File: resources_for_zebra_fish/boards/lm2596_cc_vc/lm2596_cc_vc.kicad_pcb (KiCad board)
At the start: 2 copper layers, 72.4 x 78.7 mm, 30 parts, among them J1 Vin, J2 Conn_Coaxial, J3 external_on/off, J4 to_mosfet, J5 red_vout, U1 LM2596T-3.3, U2 LM2596T-ADJ, U3 MCP602

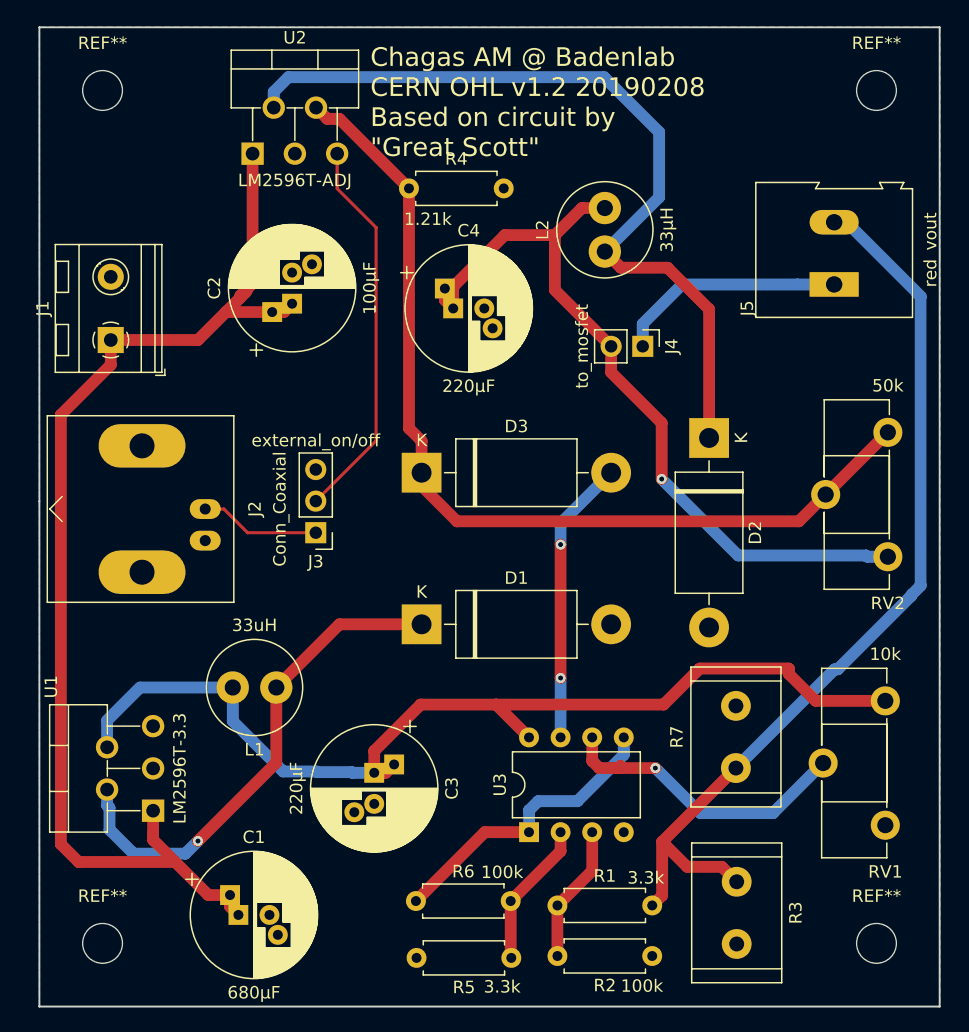
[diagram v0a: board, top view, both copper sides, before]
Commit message: new board: power supply and sync to led in one
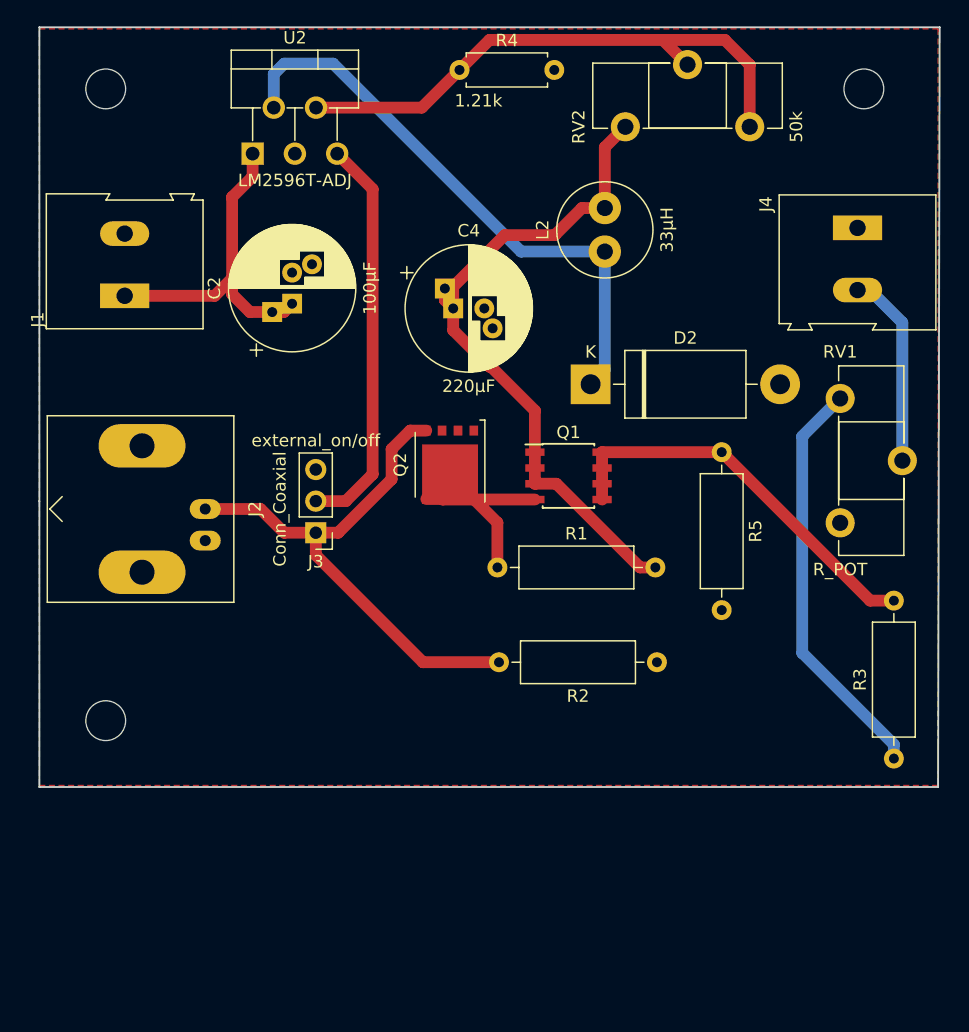
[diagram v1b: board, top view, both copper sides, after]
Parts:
- removed C1: 680µF, Capacitor_THT:CP_Radial_D10.0mm_P2.50mm_P5.00mm
- removed C3: 220µF, Capacitor_THT:CP_Radial_D10.0mm_P2.50mm_P5.00mm
- removed D1, D3: 1N5822, Diode_THT:D_DO-201AD_P15.24mm_Horizontal
- removed J5: red_vout, TerminalBlock:TerminalBlock_Altech_AK300-2_P5.00mm
- removed L1: 33uH, Inductor_THT:L_Radial_D7.5mm_P3.50mm_Fastron_07P
- removed R6: 100k, Resistor_THT:R_Axial_DIN0207_L6.3mm_D2.5mm_P7.62mm_Horizontal
- removed R7: 0.1, Resistor_THT:R_Radial_Power_L11.0mm_W7.0mm_P5.00mm
- removed the REF** at (49.5, 141.0)
- removed the REF** at (111.8, 141.0)
- removed the REF** at (111.8, 72.4)
- removed the REF** at (49.5, 72.4)
- removed U1: LM2596T-3.3, Package_TO_SOT_THT:TO-220-5_P3.4x3.7mm_StaggerOdd_Lead3.8mm_Vertical
- removed U3: MCP602, Package_DIP:DIP-8_W7.62mm
- added Q1: pchannel, Package_SO:SOIC-8_3.9x4.9mm_P1.27mm, F.Cu at (87.0, 103.4)
- added Q2: nchannel, Package_TO_SOT_SMD:TDSON-8-1, F.Cu at (77.5, 102.5)
- added REF**: MountingHole_3.2mm_M3_DIN965, MountingHole:MountingHole_3.2mm_M3_DIN965, F.Cu at (49.8, 123.1)
- added REF**: MountingHole_3.2mm_M3_DIN965, MountingHole:MountingHole_3.2mm_M3_DIN965, F.Cu at (110.7, 72.3)
- added REF**: MountingHole_3.2mm_M3_DIN965, MountingHole:MountingHole_3.2mm_M3_DIN965, F.Cu at (49.8, 72.3)
- J1: footprint TerminalBlock_RND:TerminalBlock_RND_205-00232_1x02_P5.08mm_Horizontal -> TerminalBlock:TerminalBlock_Altech_AK300-2_P5.00mm
- J4: value to_mosfet -> Vout; footprint Connector_PinHeader_2.54mm:PinHeader_1x02_P2.54mm_Vertical -> TerminalBlock:TerminalBlock_Altech_AK300-2_P5.00mm
- R1: value 3.3k -> 10k; footprint Resistor_THT:R_Axial_DIN0207_L6.3mm_D2.5mm_P7.62mm_Horizontal -> Resistor_THT:R_Axial_DIN0309_L9.0mm_D3.2mm_P12.70mm_Horizontal
- R2: value 100k -> 10k; footprint Resistor_THT:R_Axial_DIN0207_L6.3mm_D2.5mm_P7.62mm_Horizontal -> Resistor_THT:R_Axial_DIN0309_L9.0mm_D3.2mm_P12.70mm_Horizontal
- R3: value 0.1 -> R; footprint Resistor_THT:R_Radial_Power_L11.0mm_W7.0mm_P5.00mm -> Resistor_THT:R_Axial_DIN0309_L9.0mm_D3.2mm_P12.70mm_Horizontal
- R5: value 3.3k -> 1k; footprint Resistor_THT:R_Axial_DIN0207_L6.3mm_D2.5mm_P7.62mm_Horizontal -> Resistor_THT:R_Axial_DIN0309_L9.0mm_D3.2mm_P12.70mm_Horizontal
- RV1: value 10k -> R_POT
- moved R5 44.0 mm to (99.3, 101.5), turned to 270 degrees
- moved RV2 40.5 mm to (91.6, 75.3), turned to 90 degrees
- moved RV1 34.5 mm to (108.8, 97.2), turned to 0 degrees
- moved R1 27.6 mm to (81.3, 110.7)
- moved R2 23.6 mm to (94.1, 118.4)
- moved J4 19.7 mm to (110.2, 83.4)
- moved R3 16.1 mm to (113.2, 126.1), turned to 90 degrees
- moved D2 10.5 mm to (88.8, 96.0), turned to 0 degrees
- moved R4 10.4 mm to (78.2, 70.7)
- moved J1 3.73 mm to (51.3, 88.9)
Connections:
- J4 pad 1: Net-(J4-Pad1) -> GND
- J4 pad 2: Net-(C4-Pad1) -> Net-(J4-Pad2)
- R1 pad 1: Net-(R1-Pad1) -> Net-(Q1-Pad4)
- R1 pad 2: Net-(J5-Pad2) -> Net-(C4-Pad1)
- R2 pad 2: Net-(R1-Pad1) -> Net-(J2-Pad1)
- R3 pad 1: Net-(J5-Pad2) -> Net-(R3-Pad1)
- R3 pad 2: GND -> Net-(Q1-Pad5)
- R5 pad 1: Net-(R5-Pad1) -> Net-(Q1-Pad5)
- RV1 pad 1: GND -> Net-(R3-Pad1)
- RV1 pad 2: Net-(RV1-Pad2) -> Net-(J4-Pad2)
- RV1 pad 3: +3V3 -> (no net)
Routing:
- net +3V3: track 82.0 -> 0.00 mm
- net Net-(J5-Pad2): track 74.8 -> 0.00 mm
- net +24V: track 94.4 -> 26.9 mm
- net Net-(D1-Pad1): track 40.4 -> 0.00 mm, vias 1 -> 0
- net Net-(J2-Pad1): track 9.68 -> 43.5 mm
- net Net-(R3-Pad1): track 0.00 -> 33.3 mm
- net Net-(Q1-Pad5): track 0.00 -> 32.2 mm
- net Net-(R4-Pad1): track 76.1 -> 45.7 mm
- net Net-(RV1-Pad2): track 24.1 -> 0.00 mm, vias 1 -> 0
- net Net-(R6-Pad1): track 24.0 -> 0.00 mm
- net Net-(D3-Pad2): track 23.0 -> 0.00 mm, vias 2 -> 0
- net Net-(D2-Pad1): track 66.6 -> 47.1 mm
- net Net-(J4-Pad1): track 18.5 -> 0.00 mm
- net Net-(Q1-Pad4): track 0.00 -> 17.6 mm
- net Net-(J4-Pad2): track 0.00 -> 15.8 mm
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- added copper zone on F.Cu, net GND
- removed copper zone on B.Cu, net GND
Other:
- board size 72.4 x 78.7 mm -> 72.4 x 61.1 mm
- board text removed: "Chagas AM @ Badenlab CERN OHL v1.2 20190208 Based on circuit by "Great Scott""
